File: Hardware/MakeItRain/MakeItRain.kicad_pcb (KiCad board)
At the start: 4 copper layers, 151.1 x 71.1 mm, 76 parts, among them IC1 OPA2340UA_2K5, IC2 LTV-846S, J1 Conn_02x14_Odd_Even, J2 Conn_02x19_Odd_Even, J3 Conn_01x19, J4 Conn_01x01, J5 Conn_01x03, P1 Screw_Terminal_01x02, Q11 2N7000, Q12 IRF9Z34NPBF, Q13 IRF9Z34NPBF, Q14 BS250, Q15 BS250, Q16 BS250, Q17 BS250, Q2 2N7000, Q3 IRF9Z34NPBF, Q5 2N7000, Q6 IRF9Z34NPBF, Q8 2N7000, Q9 IRF9Z34NPBF, U1 MCP23008-xP, U2 178.6165.0001

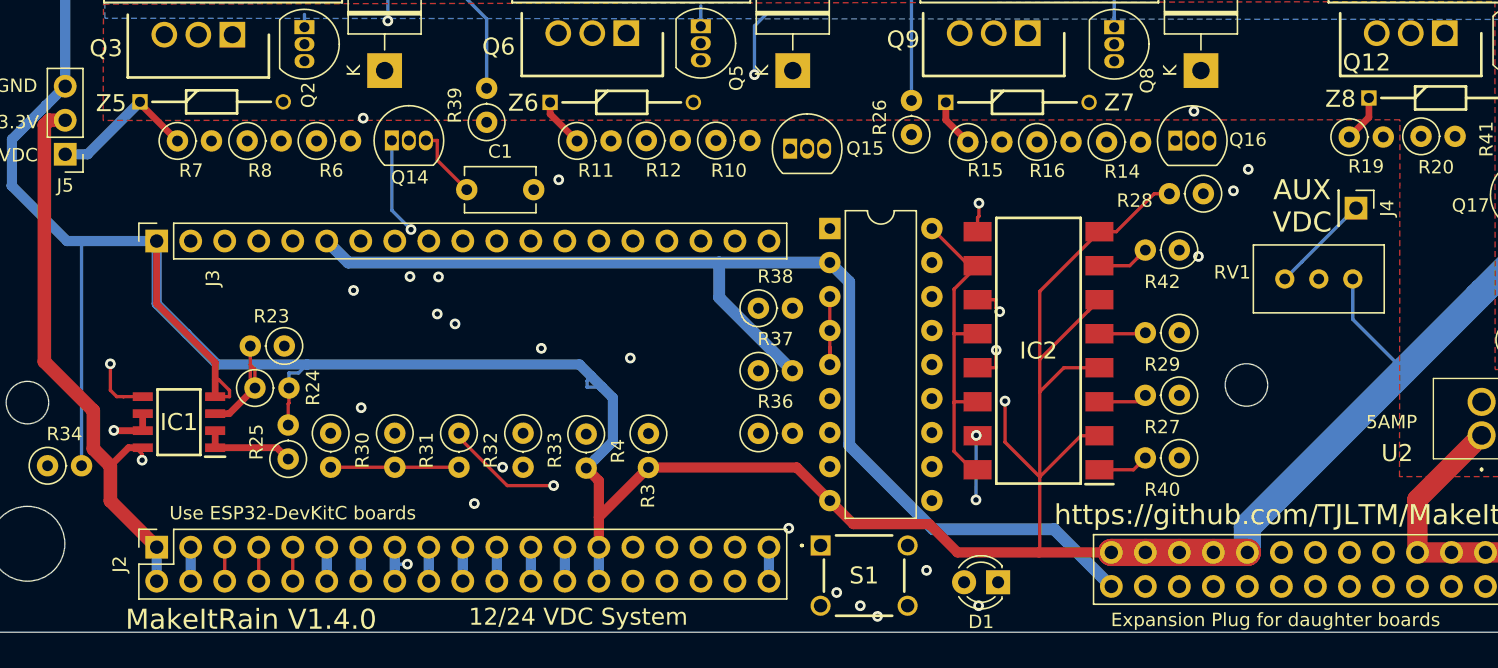
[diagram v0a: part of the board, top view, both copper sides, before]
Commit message: wip for adding RTC
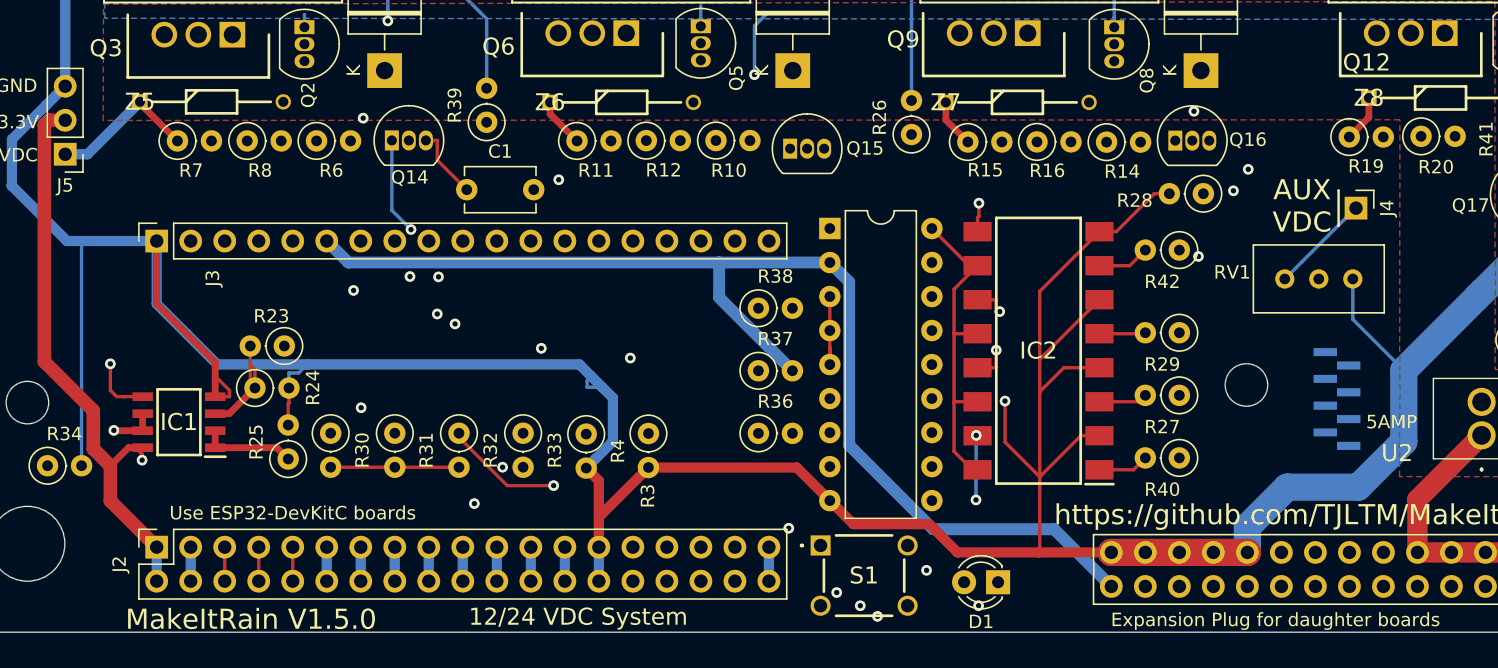
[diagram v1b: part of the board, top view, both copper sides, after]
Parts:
- added J6: Adafruit_DS3231, Connector_PinHeader_1.00mm:PinHeader_1x08_P1.00mm_Vertical_SMD_Pin1Right, B.Cu at (154.2, 109.6)
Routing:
- net D33: track 29.3 -> 25.0 mm, vias 1 -> 0
- net GND: track 441.5 -> 444.6 mm
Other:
- board text added: "MakeItRain V1.5.0"
- board text removed: "MakeItRain V1.4.0"

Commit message: wip
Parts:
- removed J6: Adafruit_DS3231, Connector_PinHeader_1.00mm:PinHeader_1x08_P1.00mm_Vertical_SMD_Pin1Right
- added C5: 0.1uF, Capacitor_THT:C_Rect_L9.0mm_W3.6mm_P7.50mm_MKT, F.Cu at (116.2, 39.9)
- added IC3: DS3231SN#, SamacSys_Parts:SOIC127P1032X265-16N, F.Cu at (121.1, 31.3)
- added U3: S8411-45R, SamacSys_Parts:S8411-45R_1, F.Cu at (106.7, 36.2)
- R10, R11, R12, R14, R15, R16, R18, R19, R20, R21, R25, R26, R27, R28, R29, R3, R30, R31, R32, R33, R36, R37, R38, R39, R4, R40, R41, R42, R6, R7, R8: footprint Resistor_THT:R_Axial_DIN0207_L6.3mm_D2.5mm_P2.54mm_Vertical -> Resistor_SMD:R_1206_3216Metric_Pad1.30x1.75mm_HandSolder
